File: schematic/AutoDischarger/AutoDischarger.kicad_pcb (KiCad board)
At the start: 4 copper layers, 50 x 50 mm, 78 parts, among them IC1 AP7375-50SA-7, IC2 PIC18F15Q40-I_SS, IC3 TLV9102SIDGSR, IC4 TLV9102SIDGSR, IC5 TLV9102SIDGSR, J1 ICSP, J2 Balance Lead, Q1 2N7002_HAMR, Q10 2N7002_HAMR, Q11 2N7002_HAMR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

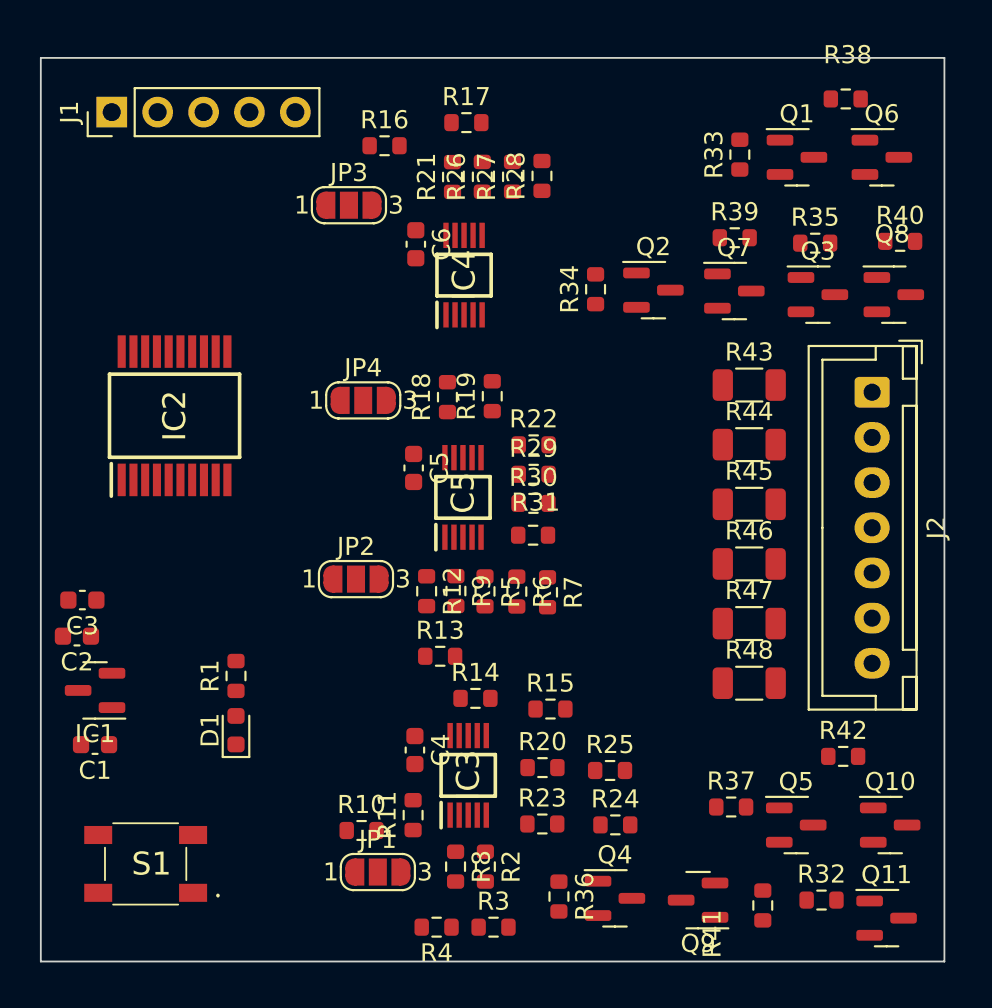
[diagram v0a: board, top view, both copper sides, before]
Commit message: Initial pcb layout
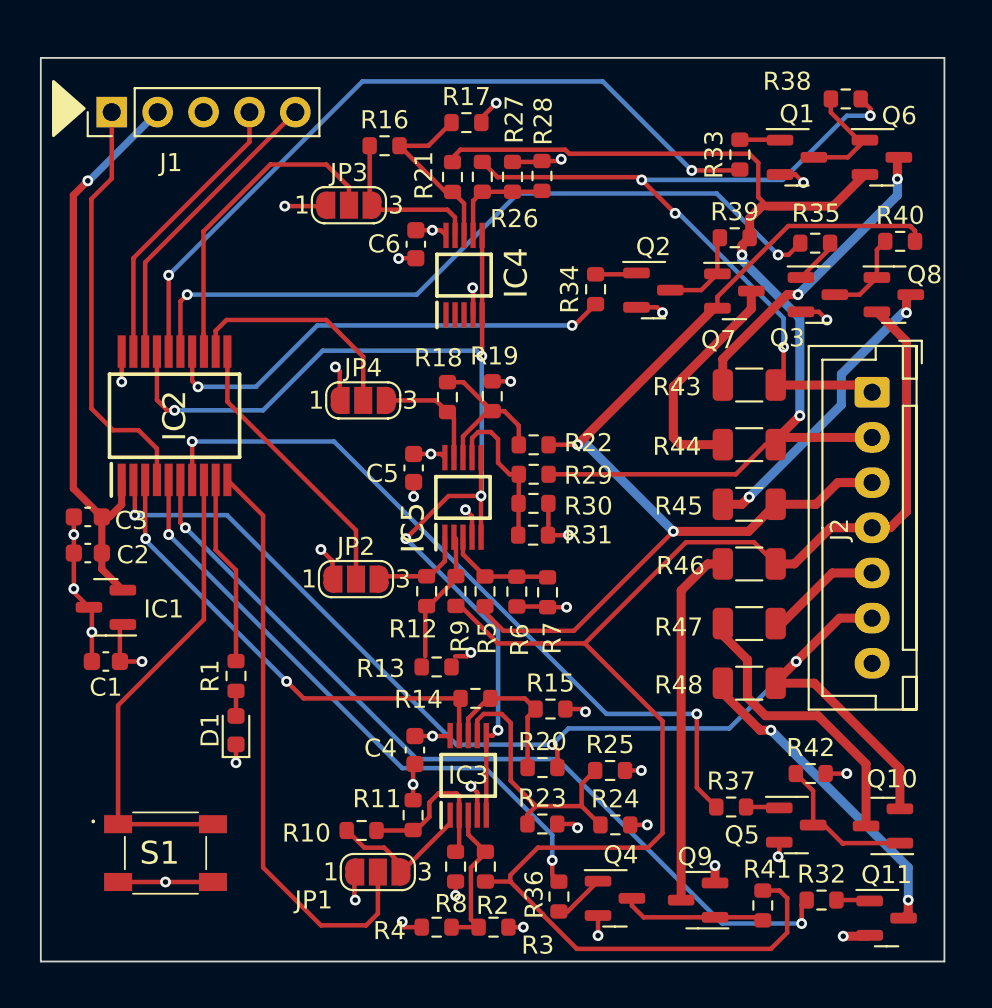
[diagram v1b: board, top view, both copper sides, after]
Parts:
- moved C1 4.64 mm to (110.6, 119.4)
- moved C2 4.64 mm to (109.6, 113.4)
- moved IC1 4.64 mm to (110.6, 116.4)
- moved C3 4.61 mm to (109.6, 111.4)
- moved R42 2.04 mm to (149.6, 125.6)
- moved S1 1.25 mm to (113.9, 130.0), turned to 0 degrees
- moved R13 0.62 mm to (128.9, 119.7)
- moved Q10 0.40 mm to (153.6, 128.5), turned to 180 degrees
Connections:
- IC2 pad 14: /Discharge Control/C3 -> /Discharge Control/C5
- IC2 pad 15: /Discharge Control/C2 -> /Discharge Control/C4
- IC2 pad 16: /Discharge Control/C1 -> /Discharge Control/C6
- IC2 pad 5: /Discharge Control/C6 -> /Discharge Control/C3
- IC2 pad 6: /Discharge Control/C5 -> /Discharge Control/C1
- IC2 pad 7: /Discharge Control/C4 -> /Discharge Control/C2
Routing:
- net /Discharge Control/VC3: track 0.00 -> 85.4 mm
- net /Discharge Control/VC1: track 0.00 -> 64.9 mm, vias 0 -> 3
- net /Voltage Sense/SHDN: track 0.00 -> 64.2 mm, vias 0 -> 5
- net /Discharge Control/VC5: track 0.00 -> 60.5 mm, vias 0 -> 2
- net /Discharge Control/VC4: track 0.00 -> 59.0 mm, vias 0 -> 2
- net GND: track 0.00 -> 57.0 mm, vias 0 -> 33
- net /Discharge Control/C1: track 0.00 -> 47.3 mm, vias 0 -> 2
- net /Discharge Control/VC6: track 0.00 -> 43.7 mm, vias 0 -> 4
- net /Discharge Control/C6: track 0.00 -> 42.3 mm, vias 0 -> 2
- net /Discharge Control/C2: track 0.00 -> 41.9 mm, vias 0 -> 2
- net /Discharge Control/C4: track 0.00 -> 41.2 mm, vias 0 -> 2
- net /Discharge Control/C3: track 0.00 -> 33.9 mm, vias 0 -> 2
- net /Voltage Sense/V_SENSE3: track 0.00 -> 32.5 mm
- net +5V: track 0.00 -> 32.3 mm, vias 0 -> 1
- net /Voltage Sense/V_SENSE2: track 0.00 -> 26.4 mm, vias 0 -> 2
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
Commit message: PCB tweaks
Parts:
- turned R38 to 180 degrees
- renumbered JP4 to JP3, JP3 to JP4
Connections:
- IC4 pad 2: unconnected-(IC4-Pad2) -> GND
- IC4 pad 3: unconnected-(IC4-Pad3) -> GND
- IC4 pad 5: /Voltage Sense/SHDN -> +8V
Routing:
- net +8V: track 19.3 -> 24.5 mm
- net /Voltage Sense/V_SENSE6: track 17.8 -> 13.4 mm
- net /Discharge Control/C6: track 42.3 -> 39.4 mm
- net /Discharge Control/VC6: track 43.7 -> 41.9 mm
- net /Discharge Control/VC5: track 60.5 -> 59.1 mm
- net GND: track 57.0 -> 58.2 mm
- net Net-(Q1-Pad3): track 6.13 -> 5.60 mm
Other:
- board text added: "AutoDischarger V1.0 QES 2022"
- board text added: "JLCJLCJLCJLC"
- board text added: "JP1=3S JP2=4S 23=enable JP3=5S 12=disable JP4=6S"

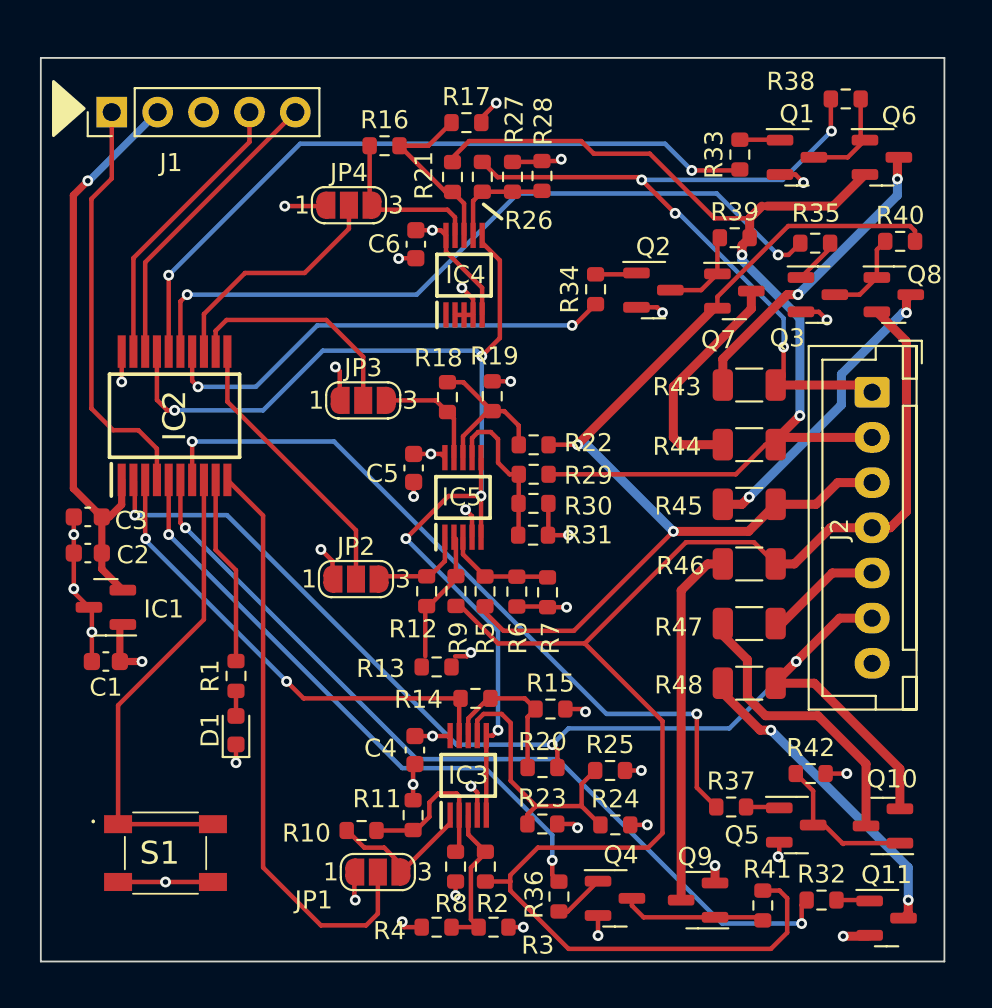
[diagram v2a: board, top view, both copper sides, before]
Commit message: Changed 5V regulator
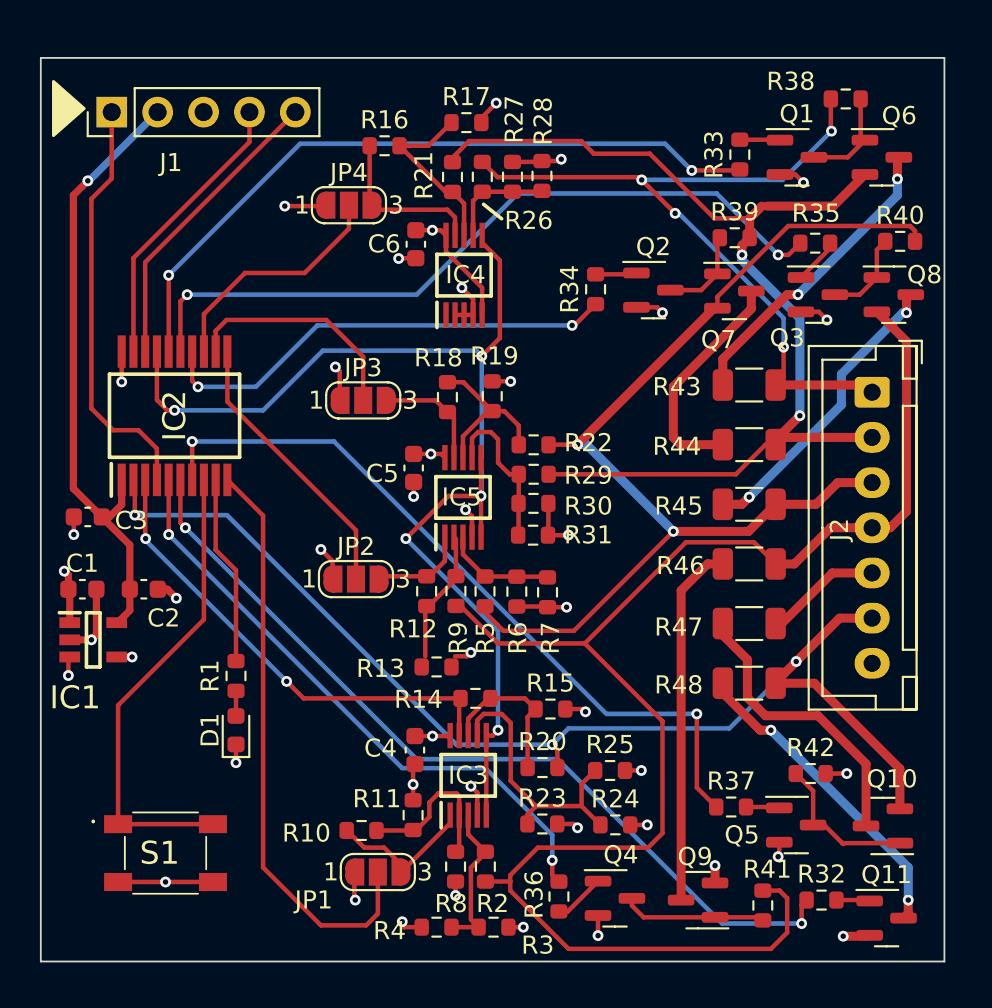
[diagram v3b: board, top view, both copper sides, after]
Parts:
- IC1: value AP7375-50SA-7 -> AP7375-50W5-7; footprint Package_TO_SOT_SMD:SOT-23 -> SamacSys_Parts:SOT95P285X140-5N
- moved C1 4.21 mm to (109.3, 115.4), turned to 0 degrees
- moved C2 3.69 mm to (112.7, 115.4), turned to 0 degrees
- moved IC1 1.93 mm to (109.9, 118.2), turned to 0 degrees
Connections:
- IC1 pad 2: +5V -> GND
- IC1 pad 3: GND -> +8V
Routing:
- net +5V: track 32.3 -> 34.6 mm
- net GND: track 58.2 -> 57.2 mm, vias 33 -> 34
- net +8V: track 24.5 -> 25.4 mm, vias 8 -> 9

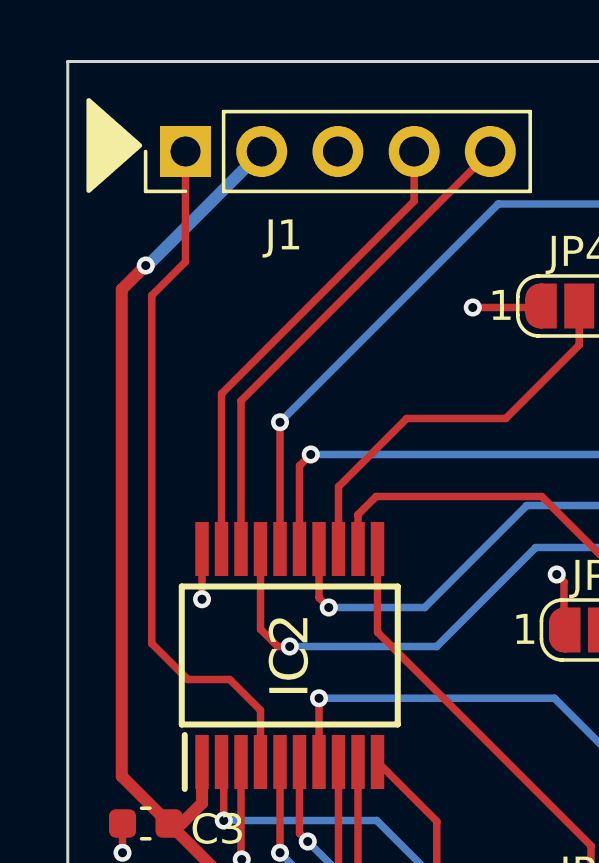
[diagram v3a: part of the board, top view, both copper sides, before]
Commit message: Added pullup to MCLR
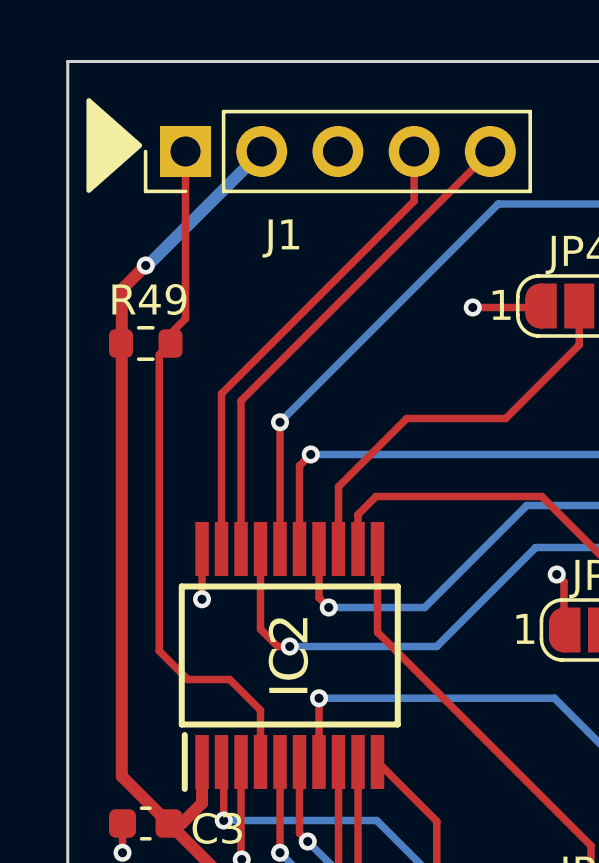
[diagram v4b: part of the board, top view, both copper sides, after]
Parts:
- added R49: 10K, Resistor_SMD:R_0603_1608Metric, F.Cu at (109.6, 95.4)
- C3: value 100 nF -> 100nF
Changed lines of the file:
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@@
+  )
+  (footprint "Resistor_SMD:R_0603_1608Metric" (layer "F.Cu")
+    (at 109.6 95.4)
+    (descr "Resistor SMD 0603 (1608 Metric), square (rectangular) end terminal, IPC_7351 nominal, (Body size source: IPC-SM-782 page 72, https://www.pcb-3d.com/wordpress/wp-content/uploads/ipc-sm-782a_amendment_1_and_2.pdf), generated with kicad-footprint-generator")
+    (tags "resistor")
+    (property "Sheetfile" "AutoDischarger.kicad_sch")
+    (property "Sheetname" "")
+    (attr smd)
+    (fp_text reference "R49" (at 0.1 -1.43) (layer "F.SilkS")
+      (effects (font (size 1 1) (thickness 0.15)))
+    )
+    (fp_text value "10K" (at 0 1.43) (layer "F.Fab")
+      (effects (font (size 1 1) (thickness 0.15)))
+    )
+    (fp_text user "${REFERENCE}" (at 0 0) (layer "F.Fab")
+      (effects (font (size 0.4 0.4) (thickness 0.06)))
+    )
+    (fp_line (start -0.237258 0.5225) (end 0.237258 0.5225) (layer "F.SilkS") (width 0.12))
+    (fp_line (start -0.237258 -0.5225) (end 0.237258 -0.5225) (layer "F.SilkS") (width 0.12))
+    (fp_line (start 1.48 -0.73) (end 1.48 0.73) (layer "F.CrtYd") (width 0.05))
+    (fp_line (start -1.48 0.73) (end -1.48 -0.73) (layer "F.CrtYd") (width 0.05))
+    (fp_line (start 1.48 0.73) (end -1.48 0.73) (layer "F.CrtYd") (width 0.05))
+    (fp_line (start -1.48 -0.73) (end 1.48 -0.73) (layer "F.CrtYd") (width 0.05))
+    (fp_line (start -0.8 -0.4125) (end 0.8 -0.4125) (layer "F.Fab") (width 0.1))
+    (fp_line (start 0.8 0.4125) (end -0.8 0.4125) (layer "F.Fab") (width 0.1))
+    (fp_line (start -0.8 0.4125) (end -0.8 -0.4125) (layer "F.Fab") (width 0.1))
+    (fp_line (start 0.8 -0.4125) (end 0.8 0.4125) (layer "F.Fab") (width 0.1))
+    (pad "1" smd roundrect (at -0.825 0) (size 0.8 0.95) (layers "F.Cu" "F.Paste" "F.Mask") (roundrect_rratio 0.25)
+      (net 3 "+5V") (pintype "passive"))
+    (pad "2" smd roundrect (at 0.825 0) (size 0.8 0.95) (layers "F.Cu" "F.Paste" "F.Mask") (roundrect_rratio 0.25)
+      (net 7 "VPP") (pintype "passive"))
+    (model "${KICAD6_3DMODEL_DIR}/Resistor_SMD.3dshapes/R_0603_1608Metric.wrl"
+      (offset (xyz 0 0 0))
+      (scale (xyz 1 1 1))
+      (rotate (xyz 0 0 0))
+    )
   )
   (footprint "Resistor_SMD:R_0603_1608Metric" (layer "F.Cu")
@@
       (effects (font (size 1 1) (thickness 0.15)))
     )
-    (fp_text value "100 nF" (at 0 1.43) (layer "F.Fab")
+    (fp_text value "100nF" (at 0 1.43) (layer "F.Fab")
       (effects (font (size 1 1) (thickness 0.15)))
     )
@@
   (segment (start 112.8 112.7) (end 112.8 112.6) (width 0.25) (layer "B.Cu") (net 6))
   (segment (start 120.6 120.5) (end 112.8 112.7) (width 0.25) (layer "B.Cu") (net 6))
-  (segment (start 110.925 92.675) (end 109.8 93.8) (width 0.25) (layer "F.Cu") (net 7))
-  (segment (start 109.8 105.4) (end 111 106.6) (width 0.25) (layer "F.Cu") (net 7))
-  (segment (start 110.925 89) (end 110.925 92.675) (width 0.25) (layer "F.Cu") (net 7))
+  (segment (start 110.425 95.4) (end 110.425 95.075) (width 0.25) (layer "F.Cu") (net 7))
+  (segment (start 110.05 95.775) (end 110.425 95.4) (width 0.25) (layer "F.Cu") (net 7))
+  (segment (start 110.925 94.575) (end 110.925 89) (width 0.25) (layer "F.Cu") (net 7))
+  (segment (start 110.425 95.075) (end 110.925 94.575) (width 0.25) (layer "F.Cu") (net 7))
+  (segment (start 110.05 105.65) (end 111 106.6) (width 0.25) (layer "F.Cu") (net 7))
   (segment (start 111 106.6) (end 112.4 106.6) (width 0.25) (layer "F.Cu") (net 7))
   (segment (start 113.425 107.625) (end 113.425 109.35) (width 0.25) (layer "F.Cu") (net 7))
+  (segment (start 110.05 105.65) (end 110.05 95.775) (width 0.25) (layer "F.Cu") (net 7))
   (segment (start 112.4 106.6) (end 113.425 107.625) (width 0.25) (layer "F.Cu") (net 7))
-  (segment (start 109.8 93.8) (end 109.8 105.4) (width 0.25) (layer "F.Cu") (net 7))
   (segment (start 145.6295 92.2255) (end 143.020799 92.2255) (width 0.25) (layer "F.Cu") (net 8))
   (segment (start 114.075 102.25) (end 114.075 98.025) (width 0.25) (layer "F.Cu") (net 8))

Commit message: Minor pcb tweaks
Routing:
- net Net-(Q7-Pad3): track 12.8 -> 12.0 mm
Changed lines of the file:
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@@
   (segment (start 129.78 91.52) (end 130.7 90.6) (width 0.25) (layer "F.Cu") (net 39))
   (segment (start 147.6625 107.4) (end 148.0625 107) (width 0.5) (layer "F.Cu") (net 39))
-  (segment (start 146.9 94.2) (end 147.2 94.2) (width 0.25) (layer "F.Cu") (net 39))
+  (segment (start 146.9 94.2) (end 147.2 94.2) (width 0.5) (layer "F.Cu") (net 39))
   (segment (start 145.46 109.04) (end 147.1 107.4) (width 0.25) (layer "F.Cu") (net 39))
   (segment (start 150.8525 94.2) (end 152.6025 92.45) (width 0.5) (layer "F.Cu") (net 39))
@@
   (segment (start 148.35783 95.3) (end 155.1 95.3) (width 0.25) (layer "F.Cu") (net 40))
   (segment (start 144.44 99.85) (end 144.44 99.21783) (width 0.25) (layer "F.Cu") (net 40))
+  (segment (start 135.105 107.4) (end 140.5 107.4) (width 0.25) (layer "F.Cu") (net 40))
   (segment (start 155.375 95.575) (end 155.375 96.15) (width 0.25) (layer "F.Cu") (net 40))
   (segment (start 131.58 116.68) (end 132.6 117.7) (width 0.25) (layer "F.Cu") (net 40))
   (segment (start 144.44 99.21783) (end 148.35783 95.3) (width 0.25) (layer "F.Cu") (net 40))
   (segment (start 131.58 116.345) (end 131.58 116.68) (width 0.25) (layer "F.Cu") (net 40))
+  (segment (start 140.6 103.5) (end 140.6 107.5) (width 0.5) (layer "F.Cu") (net 40))
   (segment (start 136.5 117.7) (end 142 112.2) (width 0.25) (layer "F.Cu") (net 40))
   (segment (start 132.6 117.7) (end 136.5 117.7) (width 0.25) (layer "F.Cu") (net 40))
@@
   (segment (start 149.9 110.7) (end 151.1 109.5) (width 0.5) (layer "F.Cu") (net 40))
   (segment (start 146.1625 112.2) (end 147.6625 110.7) (width 0.5) (layer "F.Cu") (net 40))
-  (segment (start 136.7 107.4) (end 135.105 107.4) (width 0.25) (layer "F.Cu") (net 40))
+  (segment (start 140.5 107.4) (end 140.6 107.5) (width 0.25) (layer "F.Cu") (net 40))
   (segment (start 142 112.2) (end 146.1625 112.2) (width 0.5) (layer "F.Cu") (net 40))
-  (segment (start 136.7 107.4) (end 144.25 99.85) (width 0.5) (layer "F.Cu") (net 40))
+  (segment (start 144.25 99.85) (end 140.6 103.5) (width 0.5) (layer "F.Cu") (net 40))
   (via (at 142 112.2) (size 0.6) (drill 0.3) (layers "F.Cu" "B.Cu") (net 40))
-  (via (at 136.7 107.4) (size 0.6) (drill 0.3) (layers "F.Cu" "B.Cu") (net 40))
-  (segment (start 142 112.2) (end 137.2 107.4) (width 0.5) (layer "B.Cu") (net 40))
-  (segment (start 137.2 107.4) (end 136.7 107.4) (width 0.5) (layer "B.Cu") (net 40))
+  (via (at 140.6 107.5) (size 0.6) (drill 0.3) (layers "F.Cu" "B.Cu") (net 40))
+  (segment (start 140.6 110.8) (end 140.6 107.5) (width 0.5) (layer "B.Cu") (net 40))
+  (segment (start 142 112.2) (end 140.6 110.8) (width 0.5) (layer "B.Cu") (net 40))
   (segment (start 154 112) (end 154.9 111.1) (width 0.5) (layer "F.Cu") (net 41))
   (segment (start 130.225 116.325) (end 132.3 118.4) (width 0.25) (layer "F.Cu") (net 41))
@@
   (segment (start 154.4 93.6) (end 154.4 92.7) (width 0.5) (layer "B.Cu") (net 52))
   (segment (start 148.9 99.1) (end 154.4 93.6) (width 0.5) (layer "B.Cu") (net 52))
-  (segment (start 142 104.2) (end 146.315 99.885) (width 0.5) (layer "F.Cu") (net 53))
-  (segment (start 142 107) (end 142 104.2) (width 0.5) (layer "F.Cu") (net 53))
+  (segment (start 143.4 107.4) (end 142.3 106.3) (width 0.5) (layer "F.Cu") (net 53))
   (segment (start 146.315 99.885) (end 146.315 98.9) (width 0.5) (layer "F.Cu") (net 53))
-  (segment (start 144.7375 107.4) (end 142.4 107.4) (width 0.5) (layer "F.Cu") (net 53))
-  (segment (start 142.4 107.4) (end 142 107) (width 0.5) (layer "F.Cu") (net 53))
+  (segment (start 144.7375 107.4) (end 143.4 107.4) (width 0.5) (layer "F.Cu") (net 53))
+  (segment (start 142.3 106.3) (end 142.3 103.9) (width 0.5) (layer "F.Cu") (net 53))
+  (segment (start 142.3 103.9) (end 146.315 99.885) (width 0.5) (layer "F.Cu") (net 53))
   (segment (start 145.8 110.7) (end 146.2 110.3) (width 0.5) (layer "F.Cu") (net 54))
   (segment (start 154.9 99.3375) (end 155.1375 99.1) (width 0.5) (layer "F.Cu") (net 54))
@@
   (via (at 146.2 110.3) (size 0.6) (drill 0.3) (layers "F.Cu" "B.Cu") (net 54))
   (via (at 154.9 100.1) (size 0.6) (drill 0.3) (layers "F.Cu" "B.Cu") (net 54))
+  (segment (start 151.3 103.5) (end 154.7 100.1) (width 0.5) (layer "B.Cu") (net 54))
   (segment (start 146.2 110.3) (end 151.3 105.2) (width 0.5) (layer "B.Cu") (net 54))
+  (segment (start 151.3 105.2) (end 151.3 103.5) (width 0.5) (layer "B.Cu") (net 54))
   (segment (start 154.7 100.1) (end 154.9 100.1) (width 0.5) (layer "B.Cu") (net 54))
-  (segment (start 151.3 105.2) (end 151.3 103.5) (width 0.5) (layer "B.Cu") (net 54))
-  (segment (start 151.3 103.5) (end 154.7 100.1) (width 0.5) (layer "B.Cu") (net 54))
   (segment (start 143.9 114) (end 144.7375 114) (width 0.5) (layer "F.Cu") (net 55))
   (segment (start 142.4325 115.4675) (end 143.9 114) (width 0.5) (layer "F.Cu") (net 55))
